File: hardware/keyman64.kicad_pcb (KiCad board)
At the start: 2 copper layers, 80 x 59.7 mm, 28 parts, among them IC1 ATMEGA1284P-P, P1 SERIAL, P2 CIA1, P3 KEYBOARD, P4 USER, P5 POWER, P6 USB, SW1 RESET, SW2 BOOTLOADER, U1 7400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

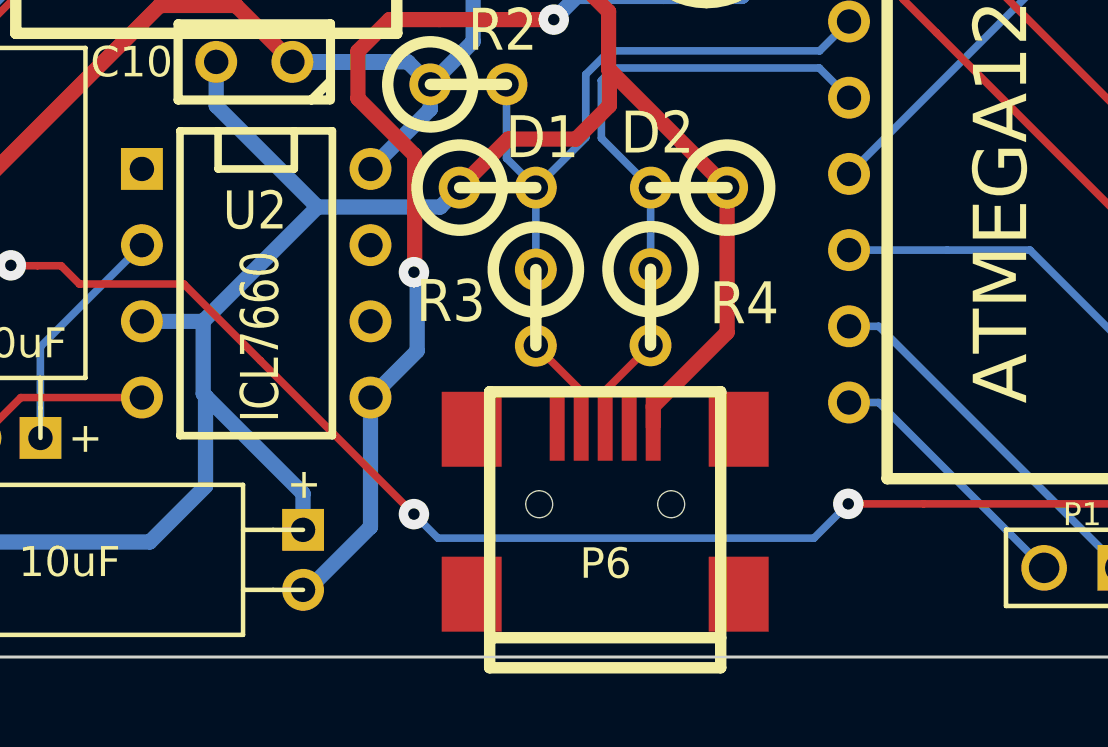
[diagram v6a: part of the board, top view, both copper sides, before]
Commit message: Hardware: Changed USB connector to mini-usb-b through-hole footprint
The footprints fit has not been verified yet, it was created based on the
datasheet for the reichelt part "USB BWM".
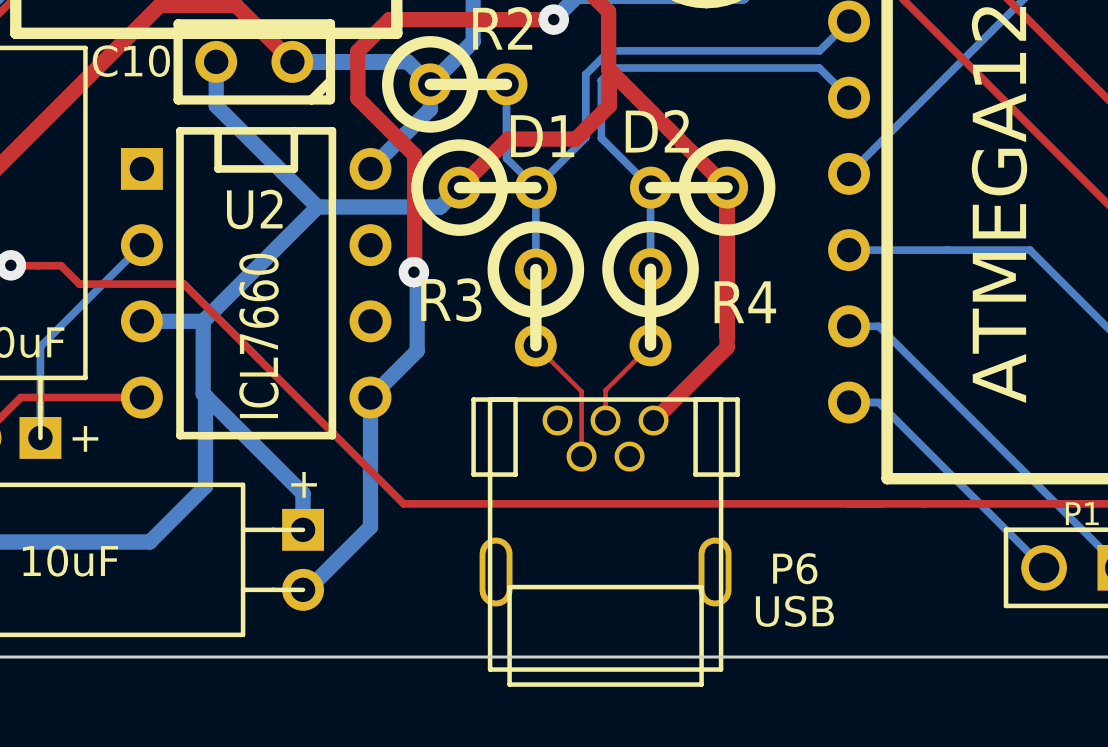
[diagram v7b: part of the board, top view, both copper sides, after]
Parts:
- P6: footprint USB_MINI_B_CORRECTED -> USB-MINI-B-H
- moved P6 1.41 mm to (132.2, 125.8), turned to 0 degrees
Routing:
- net GND: track 245.2 -> 250.2 mm
- net /~RESTORE: track 90.8 -> 94.6 mm, vias 3 -> 1
- net /D-: track 3.31 -> 4.33 mm
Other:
- net class USB added: clearance 0.15, trace_width 0.15, via_dia 1.016, via_drill 0.381
- rule trace_min: 0.254 -> 0.15

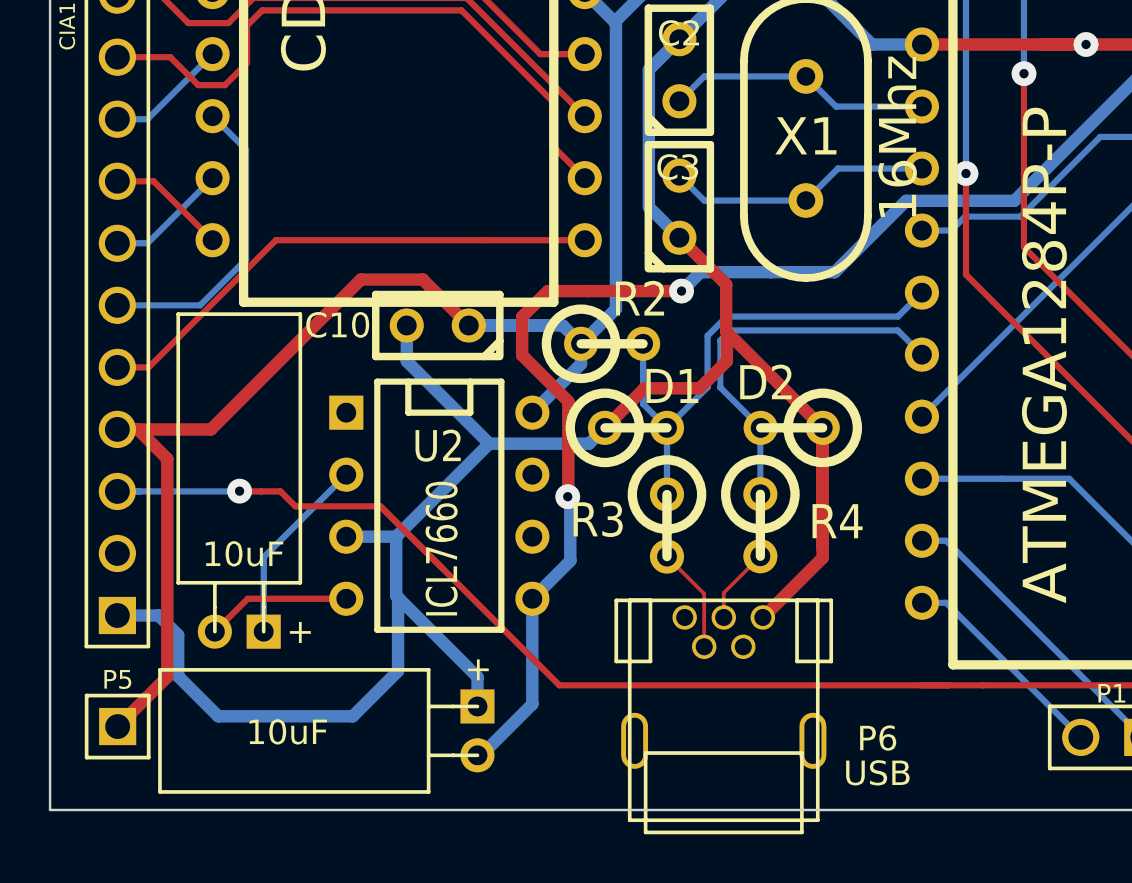
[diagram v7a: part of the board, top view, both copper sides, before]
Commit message: Hardware: Added option to power device from USB or external source
This makes it easier to use the device as a standalone keyboard controller,
i.e. without actually connecting it to a computer.

The software will support a standalone mode, in which no crosspoint switch
and consequently no meta key is required. The port used for the crosspoint
switch control will be made available as an additional user control port.
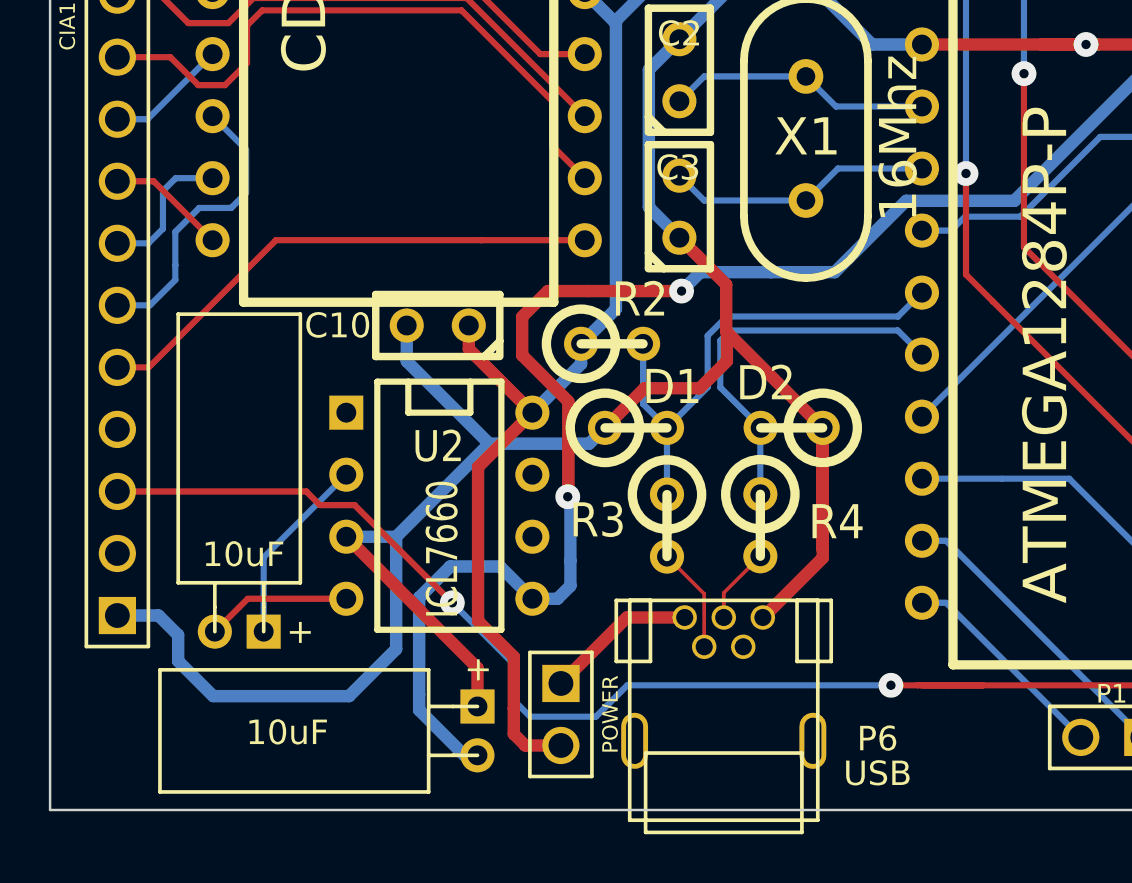
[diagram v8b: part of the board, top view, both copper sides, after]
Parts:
- P5: footprint PIN_ARRAY_1 -> pinHeader-2x1
- moved P5 18.2 mm to (125.5, 124.7), turned to 270 degrees
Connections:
- P2 pad 4: VCC -> (no net)
- P5 pad 1: VCC -> /UVCC
- P6 pad 1: (no net) -> /UVCC
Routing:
- net VCC: track 176.4 -> 157.7 mm
- net /VEE: track 84.8 -> 91.4 mm
- net /UVCC: track 0.00 -> 6.19 mm
- net GND: track 250.2 -> 251.9 mm
- net /~RESTORE: track 94.6 -> 93.4 mm, vias 1 -> 2
- net /B5: track 5.00 -> 5.91 mm
